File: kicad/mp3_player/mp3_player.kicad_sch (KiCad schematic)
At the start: 5 parts, among them U2 DFPlayer_MiniMP3

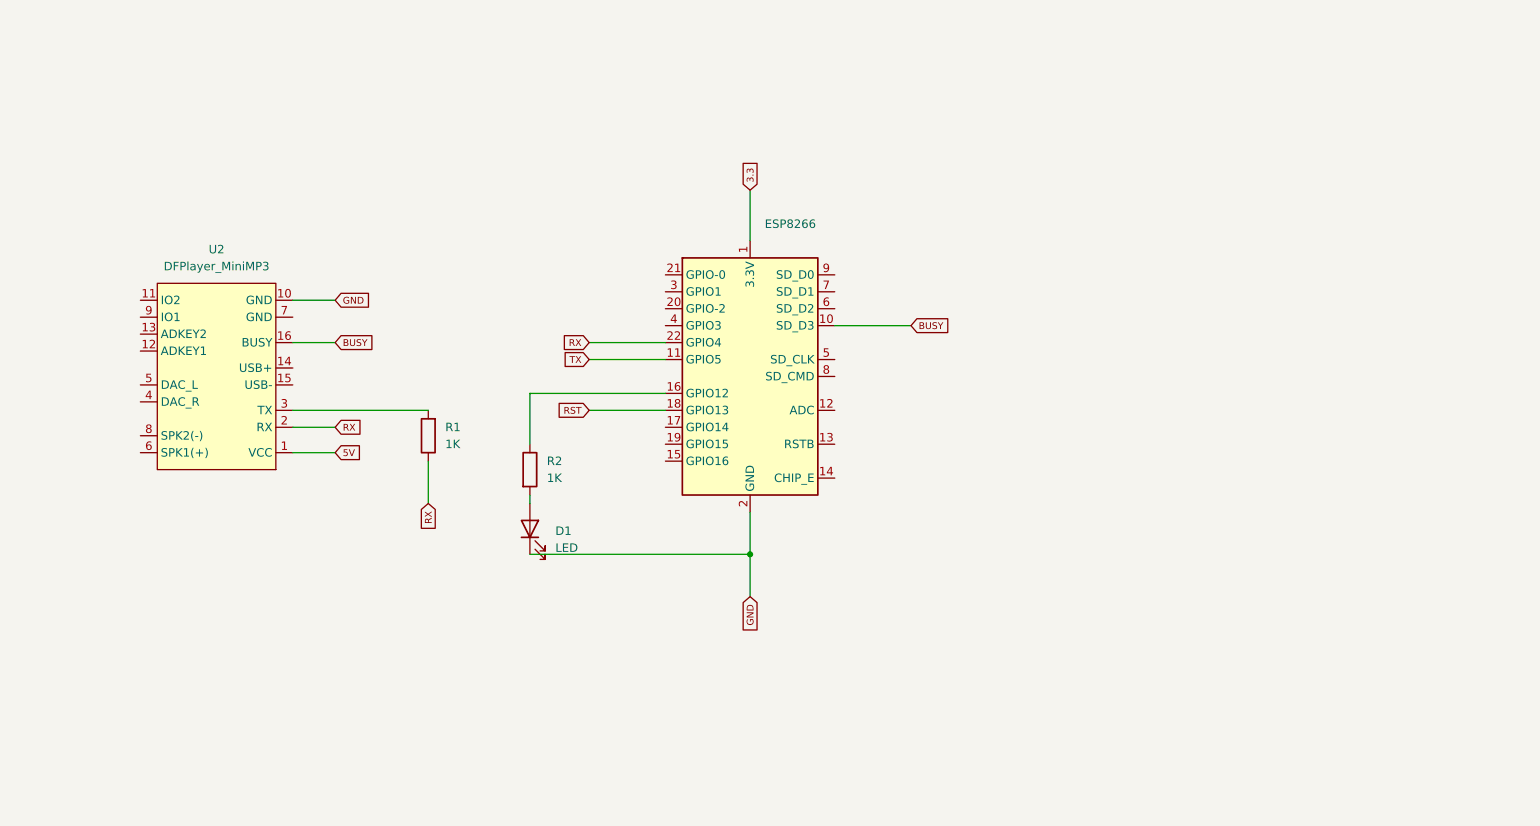
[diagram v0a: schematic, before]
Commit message: adding reset button
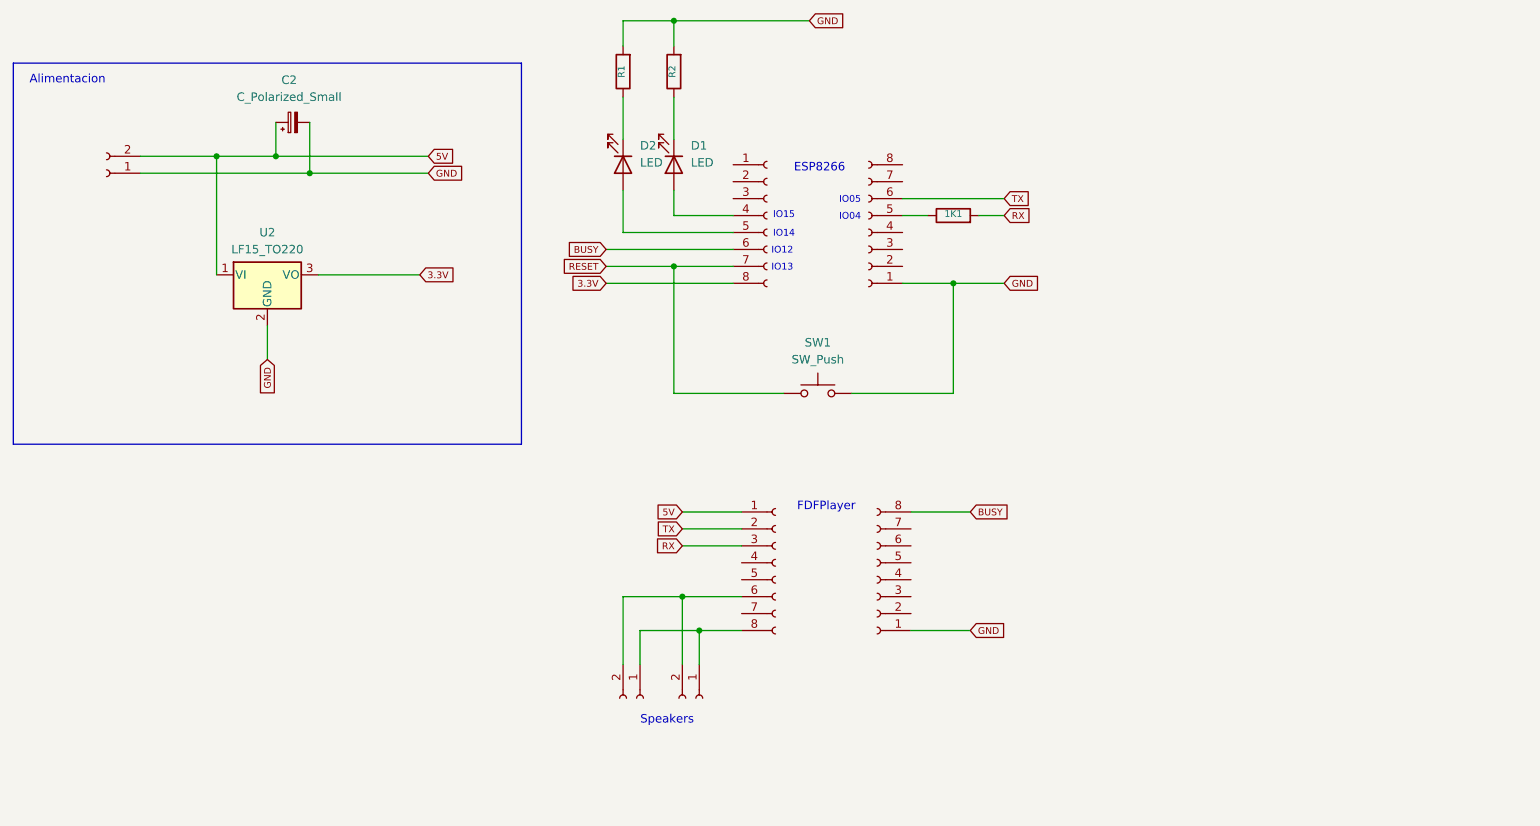
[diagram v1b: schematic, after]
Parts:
- removed ESP8266: Olimex_MOD-WIFI-ESP8266-DEV, Module:Olimex_MOD-WIFI-ESP8266-DEV, symbol MCU_Module:Olimex_MOD-WIFI-ESP8266-DEV
- removed U2: DFPlayer_MiniMP3, MCE_Modulos:DFPlayer_MiniMP3, symbol MCE-Modulos:DFPlayer_MiniMP3
- added 1K1: R, Resistor_THT:R_Axial_DIN0207_L6.3mm_D2.5mm_P7.62mm_Horizontal, symbol Device:R
- added C2: C_Polarized_Small, Capacitor_THT:CP_Radial_D7.5mm_P2.50mm, symbol Device:C_Polarized_Small
- added D2: LED, LED_THT:LED_D5.0mm, symbol Device:LED
- added J1: ESP8266-left, Connector_PinSocket_2.54mm:PinSocket_1x08_P2.54mm_Vertical, symbol Connector:Conn_01x08_Socket
- added J2: ESP8266-right, Connector_PinSocket_2.54mm:PinSocket_1x08_P2.54mm_Vertical, symbol Connector:Conn_01x08_Socket
- added J3: AC 220, Connector_JST:JST_EH_B2B-EH-A_1x02_P2.50mm_Vertical, symbol Connector:Conn_01x02_Socket
- added J4: player-left, Connector_PinSocket_2.54mm:PinSocket_1x08_P2.54mm_Vertical, symbol Connector:Conn_01x08_Socket
- added J5: player-right, Connector_PinSocket_2.54mm:PinSocket_1x08_P2.54mm_Vertical, symbol Connector:Conn_01x08_Socket
- added J6, J7: Conn_01x02_Socket, Connector_JST:JST_EH_B2B-EH-A_1x02_P2.50mm_Vertical, symbol Connector:Conn_01x02_Socket
- added SW1: SW_Push, Button_Switch_THT:SW_PUSH_6mm, symbol Switch:SW_Push
- added U2: LF15_TO220, Package_TO_SOT_THT:TO-220-3_Vertical, symbol Regulator_Linear:LF15_TO220
- D1: footprint (none) -> LED_THT:LED_D5.0mm
- R1, R2: value 1K -> R; footprint (none) -> Resistor_THT:R_Axial_DIN0207_L6.3mm_D2.5mm_P7.62mm_Horizontal
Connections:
- net 5V: now also C2.1, J3.2 (Pin_2), J4.1 (Pin_1), U2.1 (VI)
- net BUSY: now also J1.6 (Pin_6), J5.8 (Pin_8)
- net GND: now also R1.2, R2.2, C2.2, J2.1 (Pin_1), J3.1 (Pin_1), J5.1 (Pin_1), SW1.2, U2.2 (GND); no longer D1.1 (K)
- net RX: now also 1K1.2, J4.3 (Pin_3); no longer R1.1
- net TX: now also J2.6 (Pin_6), J4.2 (Pin_2)
- net at R2.1: now also D1.1 (K)
- net at D1.2 (A): now also J1.4 (Pin_4); no longer R2.2
- new net: J4.8 (Pin_8), J6.1 (Pin_1), J7.1 (Pin_1)
- new net: J4.6 (Pin_6), J6.2 (Pin_2), J7.2 (Pin_2)
- new net: 1K1.1, J2.5 (Pin_5)
- new net: D2.1 (K), R1.1
- new net: D2.2 (A), J1.5 (Pin_5)
- new net 3.3V: J1.8 (Pin_8), U2.3 (VO)
- new net RESET: J1.7 (Pin_7), SW1.1
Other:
- note added: "Alimentacion"
- note added: "ESP8266"
- note added: "FDFPlayer"
- note added: "IO04"
- note added: "IO05"
- note added: "IO12"
- note added: "IO13"
- note added: "IO14"
- note added: "IO15"
- note added: "Speakers"

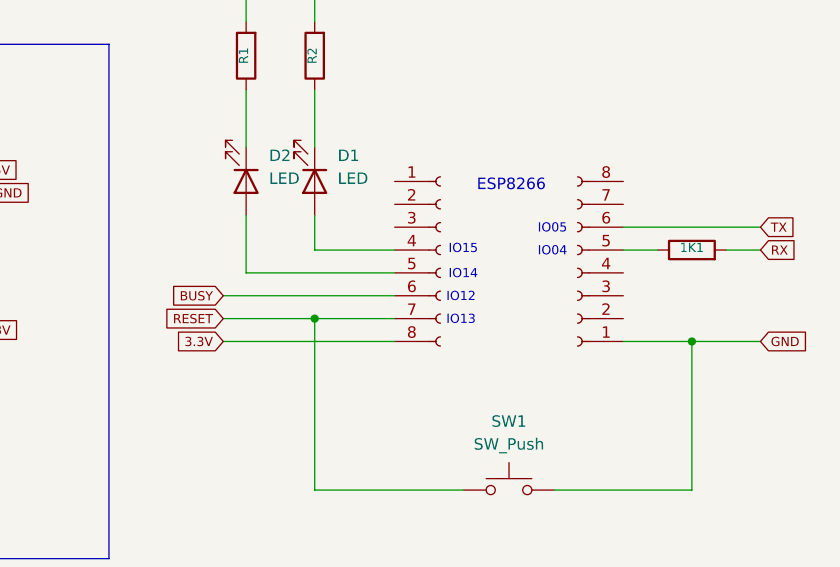
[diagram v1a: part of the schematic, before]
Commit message: wifimanager only needs to be started once
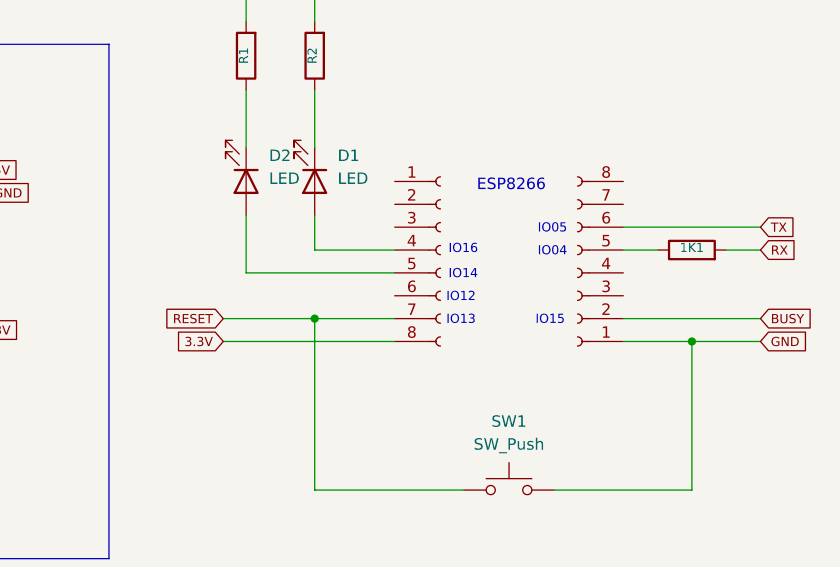
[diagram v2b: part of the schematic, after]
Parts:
- SW1: footprint Button_Switch_THT:SW_PUSH_6mm -> Button_Switch_THT:SW_PUSH_6mm_H4.3mm
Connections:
- net BUSY: now also J2.2 (Pin_2); no longer J1.6 (Pin_6)
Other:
- note added: "IO16"
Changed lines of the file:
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@@
-	(wire
-		(pts
-			(xy 147.32 74.93) (xy 166.37 74.93)
-		)
-		(stroke
-			(width 0)
-			(type default)
-		)
-	)
 	(wire
 		(pts
@@
 		(pts
 			(xy 97.79 60.96) (xy 120.65 60.96)
+		)
+		(stroke
+			(width 0)
+			(type default)
+		)
+	)
+	(wire
+		(pts
+			(xy 191.77 77.47) (xy 207.01 77.47)
 		)
 		(stroke
@@
 	(text "IO15"
 		(exclude_from_sim no)
+		(at 183.642 77.724 0)
+		(effects
+			(font
+				(size 1.016 1.016)
+			)
+		)
+	)
+	(text "IO16"
+		(exclude_from_sim no)
 		(at 173.99 69.85 0)
 		(effects
@@
 	(global_label "BUSY"
 		(shape input)
-		(at 147.32 74.93 180)
-		(fields_autoplaced yes)
-		(effects
-			(font
-				(size 1.016 1.016)
-			)
-			(justify right)
-		)
-		(property "Intersheetrefs" "${INTERSHEET_REFS}"
-			(at 141.0132 74.93 0)
-			(effects
-				(font
-					(size 1.27 1.27)
-				)
-				(justify right)
+		(at 207.01 77.47 0)
+		(fields_autoplaced yes)
+		(effects
+			(font
+				(size 1.016 1.016)
+			)
+			(justify left)
+		)
+		(property "Intersheetrefs" "${INTERSHEET_REFS}"
+			(at 213.3168 77.47 0)
+			(effects
+				(font
+					(size 1.27 1.27)
+				)
+				(justify left)
 				(hide yes)
 			)
@@
 			)
 		)
-		(property "Footprint" "Button_Switch_THT:SW_PUSH_6mm"
+		(property "Footprint" "Button_Switch_THT:SW_PUSH_6mm_H4.3mm"
 			(at 179.07 91.44 0)
 			(effects

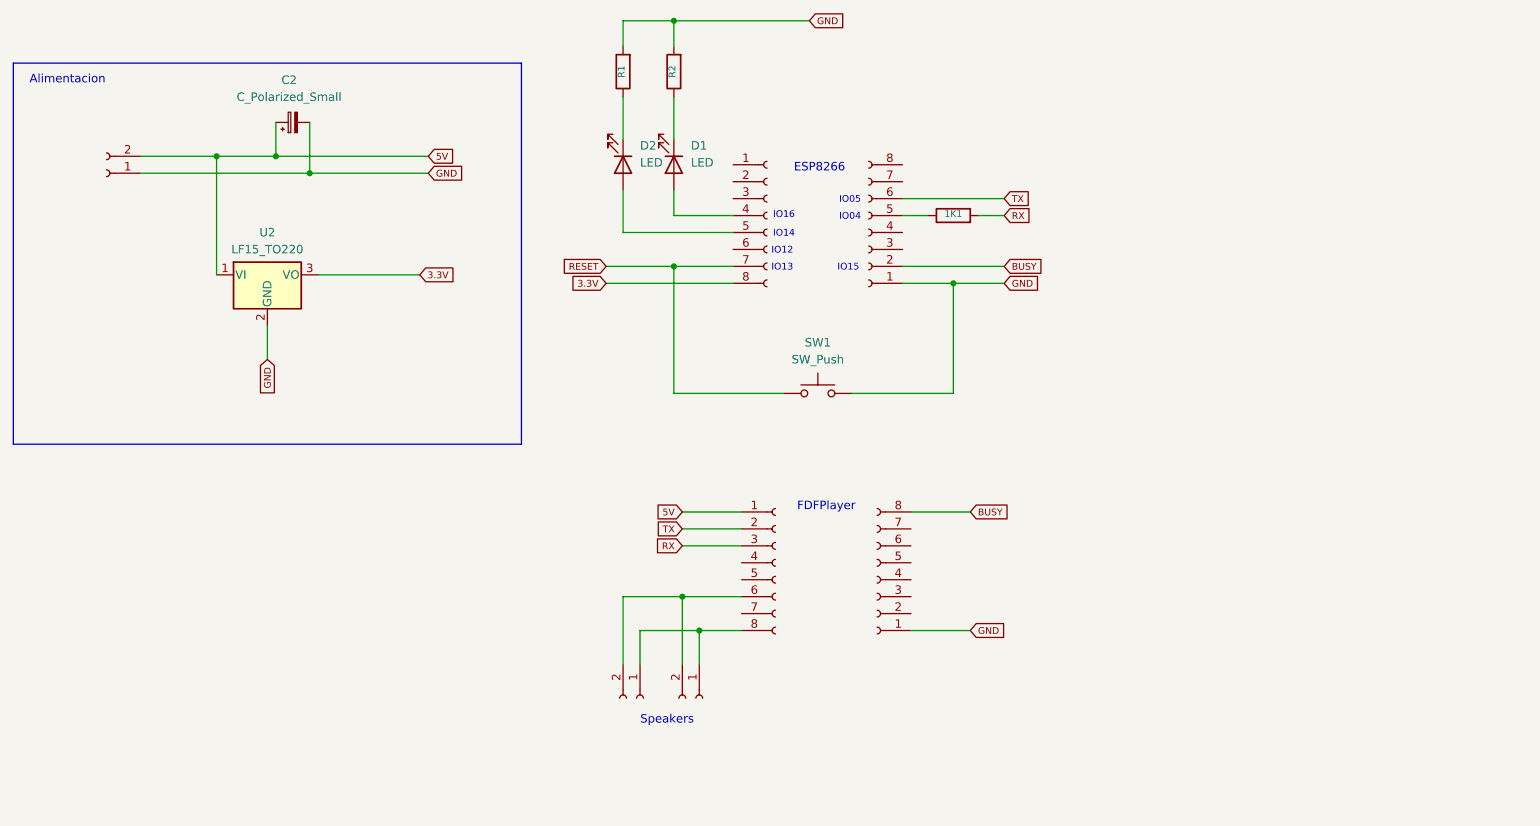
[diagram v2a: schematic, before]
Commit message: many changes. Main workaround to loop on faulty player
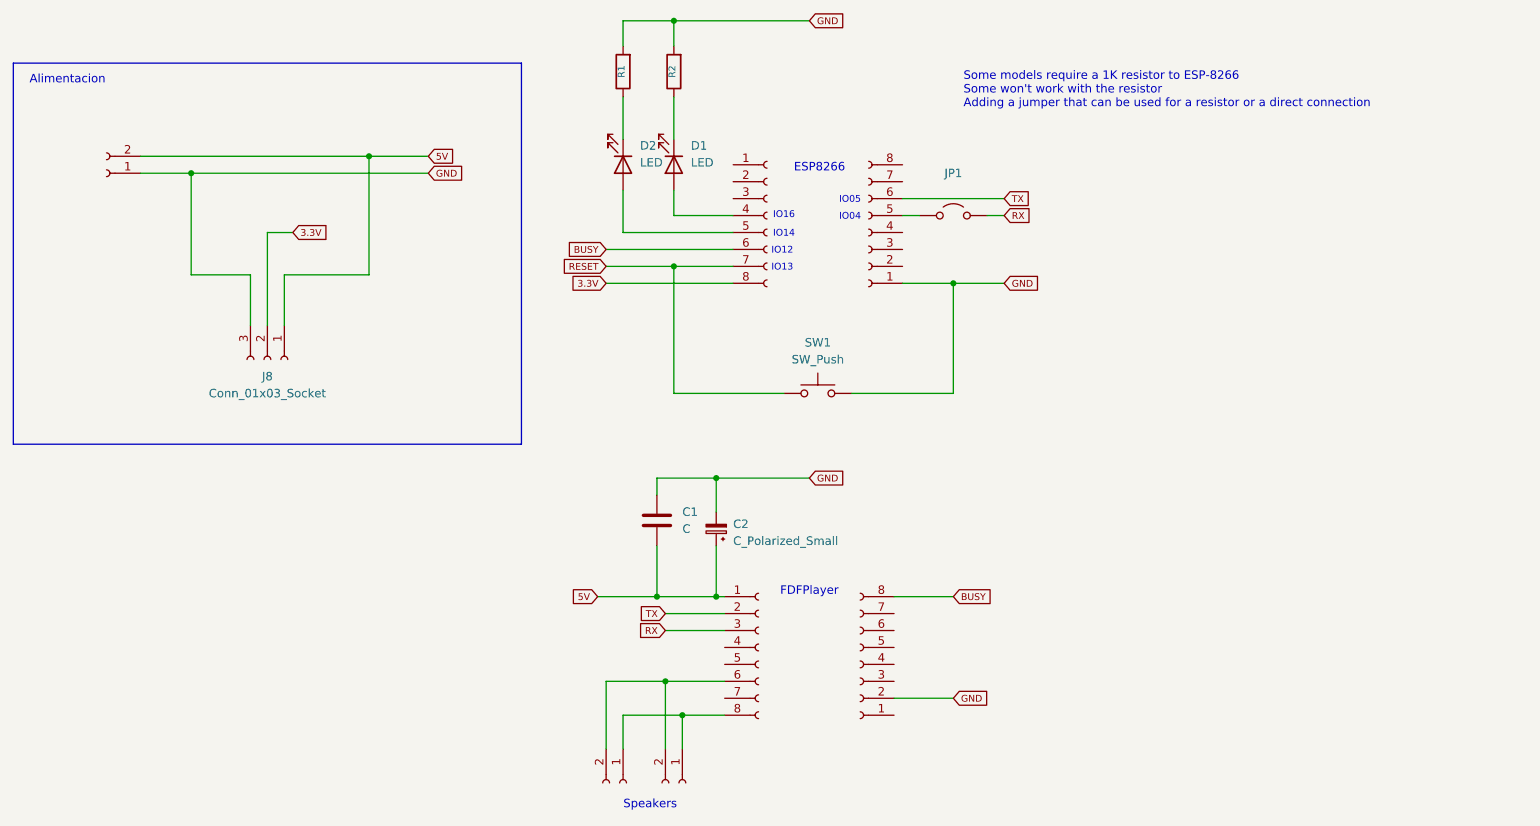
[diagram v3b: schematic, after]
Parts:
- removed 1K1: R, Resistor_THT:R_Axial_DIN0207_L6.3mm_D2.5mm_P7.62mm_Horizontal, symbol Device:R
- removed U2: LF15_TO220, Package_TO_SOT_THT:TO-220-3_Vertical, symbol Regulator_Linear:LF15_TO220
- added C1: C, Capacitor_THT:C_Disc_D3.0mm_W1.6mm_P2.50mm, symbol Device:C
- added J8: Conn_01x03_Socket, Connector_PinSocket_2.54mm:PinSocket_1x03_P2.54mm_Vertical, symbol Connector:Conn_01x03_Socket
- added JP1: Jumper_2_Open, TestPoint:TestPoint_2Pads_Pitch5.08mm_Drill1.3mm, symbol Jumper:Jumper_2_Open
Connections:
- net 3.3V: now also J8.2 (Pin_2)
- net 5V: now also C1.1, J8.1 (Pin_1)
- net BUSY: now also J1.6 (Pin_6); no longer J2.2 (Pin_2)
- net GND: now also J5.2 (Pin_2), C1.2, J8.3 (Pin_3); no longer J5.1 (Pin_1)
- net RX: now also JP1.2 (B)
- net at J2.5 (Pin_5): now also JP1.1 (A)
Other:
- note added: "Some models require a 1K resistor to ESP-8266 Some won't work with the resistor Adding a jumper that can be used for a resistor or a direct connection"
- note removed: "IO15"
- moved on the sheet: C2
